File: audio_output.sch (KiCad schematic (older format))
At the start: 21 parts, among them U8 OPA1664

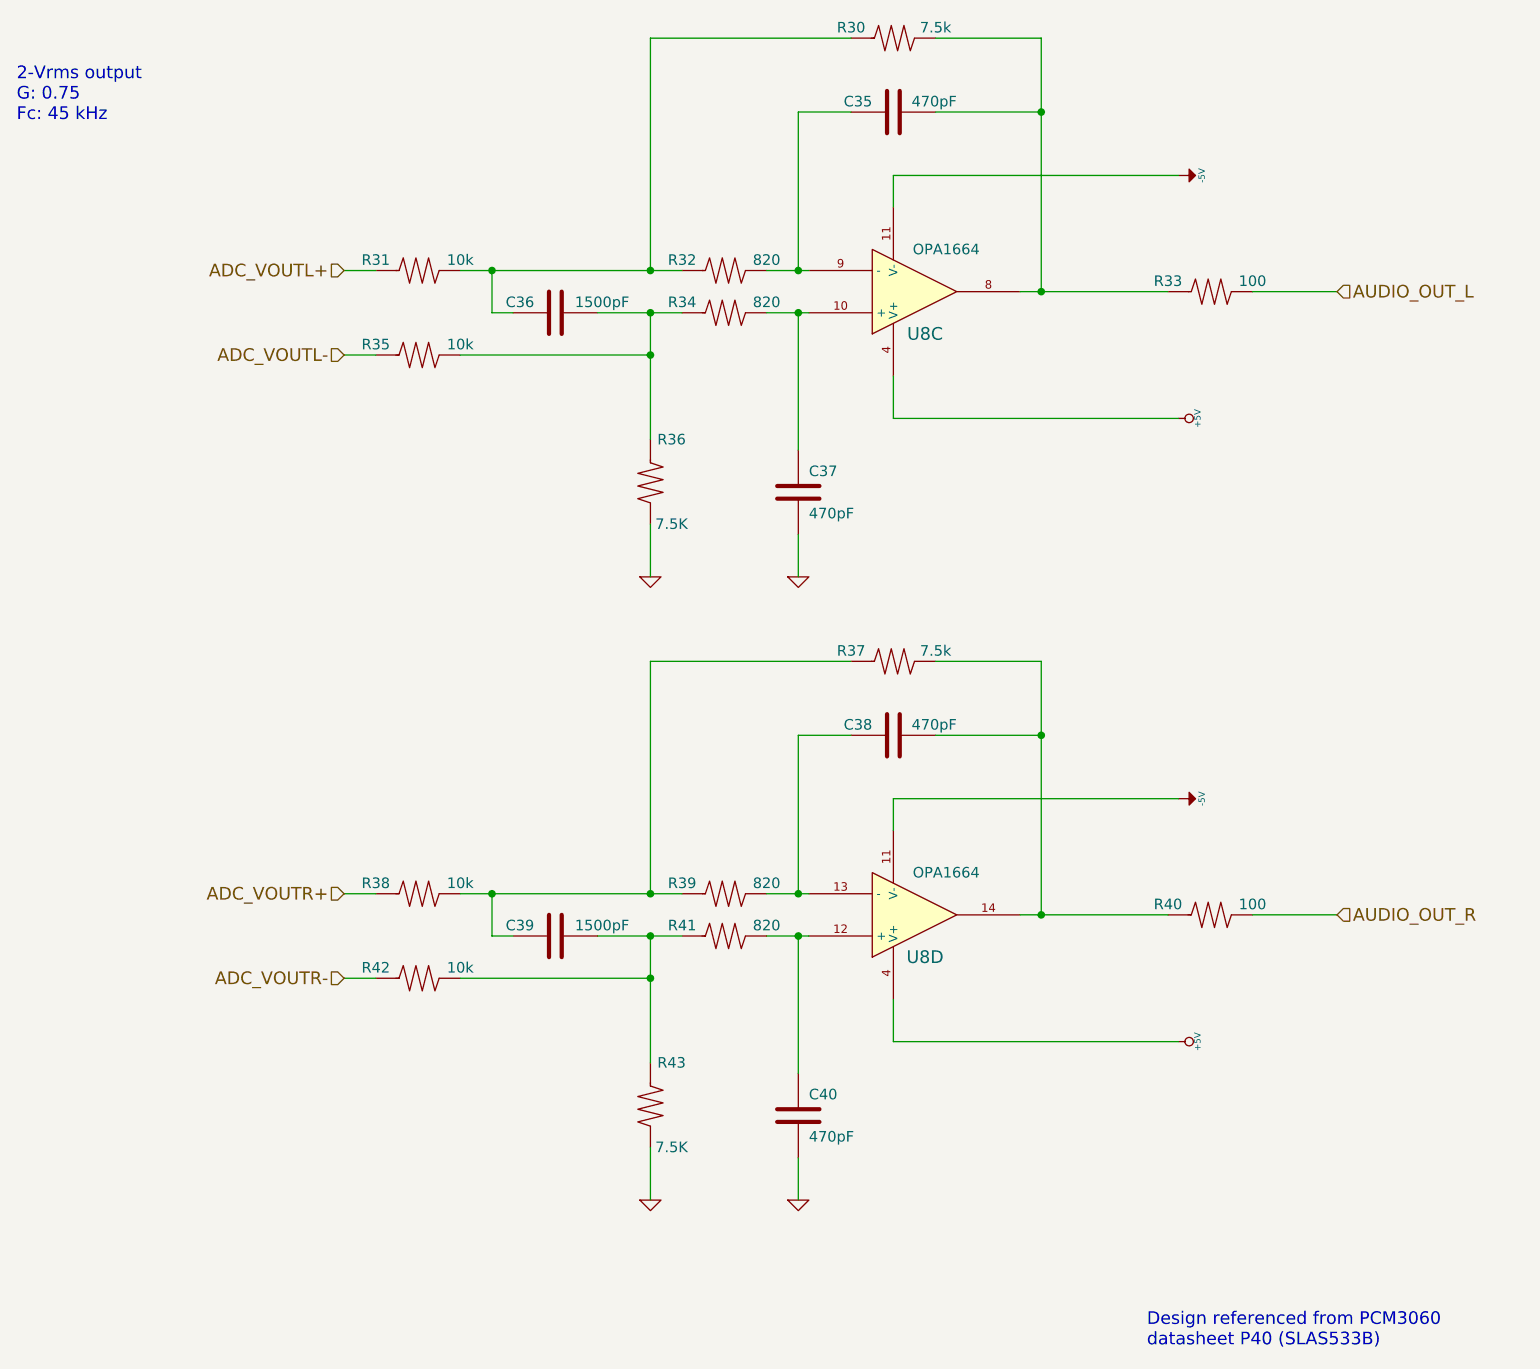
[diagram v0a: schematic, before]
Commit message: Added lib parts, adding atmega32u4 to board schematic, adding new CODED crystal
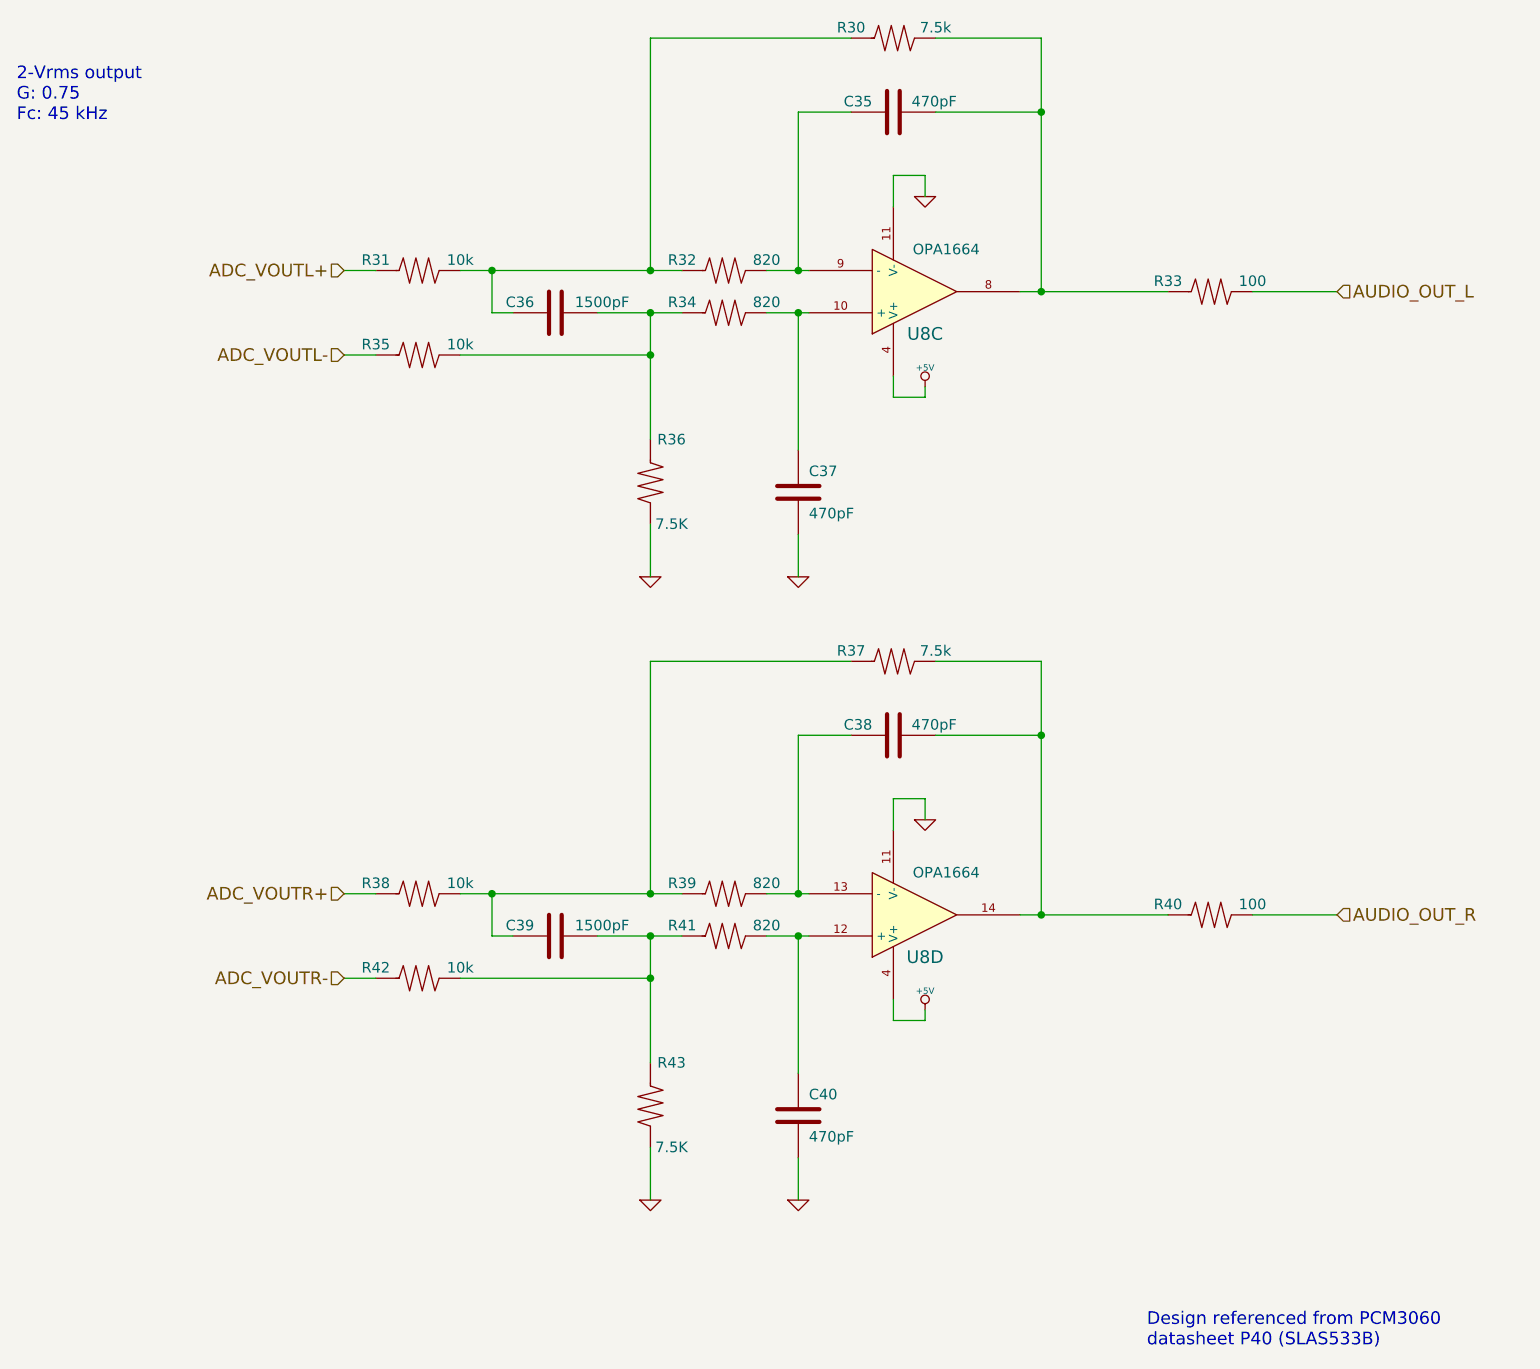
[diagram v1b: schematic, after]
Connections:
- net -5V is gone; now on net GND: U8.11 (V-), U8.11 (V-)
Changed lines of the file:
@@
 LIBS:muse_mini
 LIBS:musev2
+LIBS:autodrive
+LIBS:atx24
+LIBS:musev3-cache
 EELAYER 25 0
 EELAYER END
@@
 	2550 1950 2700 1950
 Wire Wire Line
-	4550 1950 4750 1950
+	4550 1950 4700 1950
+Wire Wire Line
+	4700 1950 4750 1950
 Wire Wire Line
 	5150 1500 5150 1650
-$Comp
-L -5V #PWR097
-U 1 1 5A4A0210
-P 6500 1500
-F 0 "#PWR097" H 6500 1640 20  0001 C CNN
-F 1 "-5V" H 6500 1610 30  0000 C CNN
-F 2 "" H 6500 1500 60  0000 C CNN
-F 3 "" H 6500 1500 60  0000 C CNN
-	1    6500 1500
-	0    1    1    0
-$EndComp
 $Comp
 L +5V #PWR098
 U 1 1 5A4A0216
-P 6500 2650
-F 0 "#PWR098" H 6500 2740 20  0001 C CNN
-F 1 "+5V" H 6500 2740 30  0000 C CNN
-F 2 "" H 6500 2650 60  0000 C CNN
-F 3 "" H 6500 2650 60  0000 C CNN
-	1    6500 2650
-	0    1    1    0
+P 5300 2500
+F 0 "#PWR098" H 5300 2590 20  0001 C CNN
+F 1 "+5V" H 5300 2590 30  0000 C CNN
+F 2 "" H 5300 2500 60  0000 C CNN
+F 3 "" H 5300 2500 60  0000 C CNN
+	1    5300 2500
+	1    0    0    -1
 $EndComp
 $Comp
@@
 Connection ~ 4700 1950
 Wire Wire Line
-	5150 2650 6500 2650
-Wire Wire Line
-	5150 1500 6500 1500
-Wire Wire Line
-	5750 2050 6450 2050
-Wire Wire Line
-	5850 850  5850 2050
+	5150 2550 5300 2550
+Wire Wire Line
+	5150 1500 5300 1500
+Wire Wire Line
+	5750 2050 5850 2050
+Wire Wire Line
+	5850 2050 6450 2050
+Wire Wire Line
+	5850 850  5850 1200
+Wire Wire Line
+	5850 1200 5850 2050
 Wire Wire Line
 	5850 1200 5350 1200
@@
 	4700 2800 4700 2150
 Wire Wire Line
-	4550 2150 4750 2150
+	4550 2150 4700 2150
+Wire Wire Line
+	4700 2150 4750 2150
 Connection ~ 4700 2150
 $Comp
@@
 $EndComp
 Wire Wire Line
-	3100 1950 4150 1950
+	3100 1950 3250 1950
+Wire Wire Line
+	3250 1950 4000 1950
+Wire Wire Line
+	4000 1950 4150 1950
 $Comp
 L R R31
@@
 $EndComp
 Wire Wire Line
-	3750 2150 4150 2150
+	3750 2150 4000 2150
+Wire Wire Line
+	4000 2150 4150 2150
 Wire Wire Line
 	3250 2150 3350 2150
@@
 Connection ~ 4000 1950
 Wire Wire Line
-	4000 2150 4000 2750
+	4000 2150 4000 2350
+Wire Wire Line
+	4000 2350 4000 2750
 $Comp
 L R R36
@@
 	2550 4900 2700 4900
 Wire Wire Line
-	4550 4900 4750 4900
-Wire Wire Line
-	5150 4450 5150 4600
-$Comp
-L -5V #PWR0101
-U 1 1 5A4A1169
-P 6500 4450
-F 0 "#PWR0101" H 6500 4590 20  0001 C CNN
-F 1 "-5V" H 6500 4560 30  0000 C CNN
-F 2 "" H 6500 4450 60  0000 C CNN
-F 3 "" H 6500 4450 60  0000 C CNN
-	1    6500 4450
-	0    1    1    0
-$EndComp
-$Comp
-L +5V #PWR0102
-U 1 1 5A4A116F
-P 6500 5600
-F 0 "#PWR0102" H 6500 5690 20  0001 C CNN
-F 1 "+5V" H 6500 5690 30  0000 C CNN
-F 2 "" H 6500 5600 60  0000 C CNN
-F 3 "" H 6500 5600 60  0000 C CNN
-	1    6500 5600
-	0    1    1    0
-$EndComp
+	4550 4900 4700 4900
+Wire Wire Line
+	4700 4900 4750 4900
 $Comp
 L C C38
@@
 Connection ~ 4700 4900
 Wire Wire Line
-	5150 5600 6500 5600
-Wire Wire Line
-	5150 4450 6500 4450
-Wire Wire Line
-	5750 5000 6450 5000
-Wire Wire Line
-	5850 3800 5850 5000
+	5750 5000 5850 5000
+Wire Wire Line
+	5850 5000 6450 5000
+Wire Wire Line
+	5850 3800 5850 4150
+Wire Wire Line
+	5850 4150 5850 5000
 Wire Wire Line
 	5850 4150 5350 4150
@@
 	4700 5750 4700 5100
 Wire Wire Line
-	4550 5100 4750 5100
+	4550 5100 4700 5100
+Wire Wire Line
+	4700 5100 4750 5100
 Connection ~ 4700 5100
 $Comp
@@
 $EndComp
 Wire Wire Line
-	3100 4900 4150 4900
+	3100 4900 3250 4900
+Wire Wire Line
+	3250 4900 4000 4900
+Wire Wire Line
+	4000 4900 4150 4900
 $Comp
 L R R38
@@
 $EndComp
 Wire Wire Line
-	3750 5100 4150 5100
+	3750 5100 4000 5100
+Wire Wire Line
+	4000 5100 4150 5100
 Wire Wire Line
 	3250 5100 3350 5100
@@
 Connection ~ 4000 4900
 Wire Wire Line
-	4000 5100 4000 5700
+	4000 5100 4000 5300
+Wire Wire Line
+	4000 5300 4000 5700
 $Comp
 L R R43
@@
 	4000 6350 4000 6100
 Wire Wire Line
-	5150 5400 5150 5600
-Wire Wire Line
-	5150 2450 5150 2650
+	5150 2450 5150 2550
 Text Notes 1000 1250 0    60   ~ 0
 2-Vrms output\nG: 0.75\nFc: 45 kHz
 Text Notes 6350 7050 0    60   ~ 0
 Design referenced from PCM3060\ndatasheet P40 (SLAS533B)
+Wire Wire Line
+	5300 2550 5300 2500
+$Comp
+L GND #PWR?
+U 1 1 5B2B6AAE
+P 5300 1600
+F 0 "#PWR?" H 5300 1600 30  0001 C CNN
+F 1 "GND" H 5300 1530 30  0001 C CNN
+F 2 "" H 5300 1600 60  0000 C CNN
+F 3 "" H 5300 1600 60  0000 C CNN
+	1    5300 1600
+	1    0    0    -1
+$EndComp
+Wire Wire Line
+	5300 1500 5300 1600
+$Comp
+L +5V #PWR?
+U 1 1 5B2B6DC6
+P 5300 5450
+F 0 "#PWR?" H 5300 5540 20  0001 C CNN
+F 1 "+5V" H 5300 5540 30  0000 C CNN
+F 2 "" H 5300 5450 60  0000 C CNN
+F 3 "" H 5300 5450 60  0000 C CNN
+	1    5300 5450
+	1    0    0    -1
+$EndComp
+Wire Wire Line
+	5150 5500 5300 5500
+Wire Wire Line
+	5150 5400 5150 5500
+Wire Wire Line
+	5300 5500 5300 5450
+Wire Wire Line
+	5150 4450 5150 4600
+Wire Wire Line
+	5150 4450 5300 4450
+$Comp
+L GND #PWR?
+U 1 1 5B2B6F6A
+P 5300 4550
+F 0 "#PWR?" H 5300 4550 30  0001 C CNN
+F 1 "GND" H 5300 4480 30  0001 C CNN
+F 2 "" H 5300 4550 60  0000 C CNN
+F 3 "" H 5300 4550 60  0000 C CNN
+	1    5300 4550
+	1    0    0    -1
+$EndComp
+Wire Wire Line
+	5300 4450 5300 4550
 $EndSCHEMATC
